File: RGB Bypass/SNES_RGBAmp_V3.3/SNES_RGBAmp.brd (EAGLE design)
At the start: 31 x 18.6 mm, 25 parts

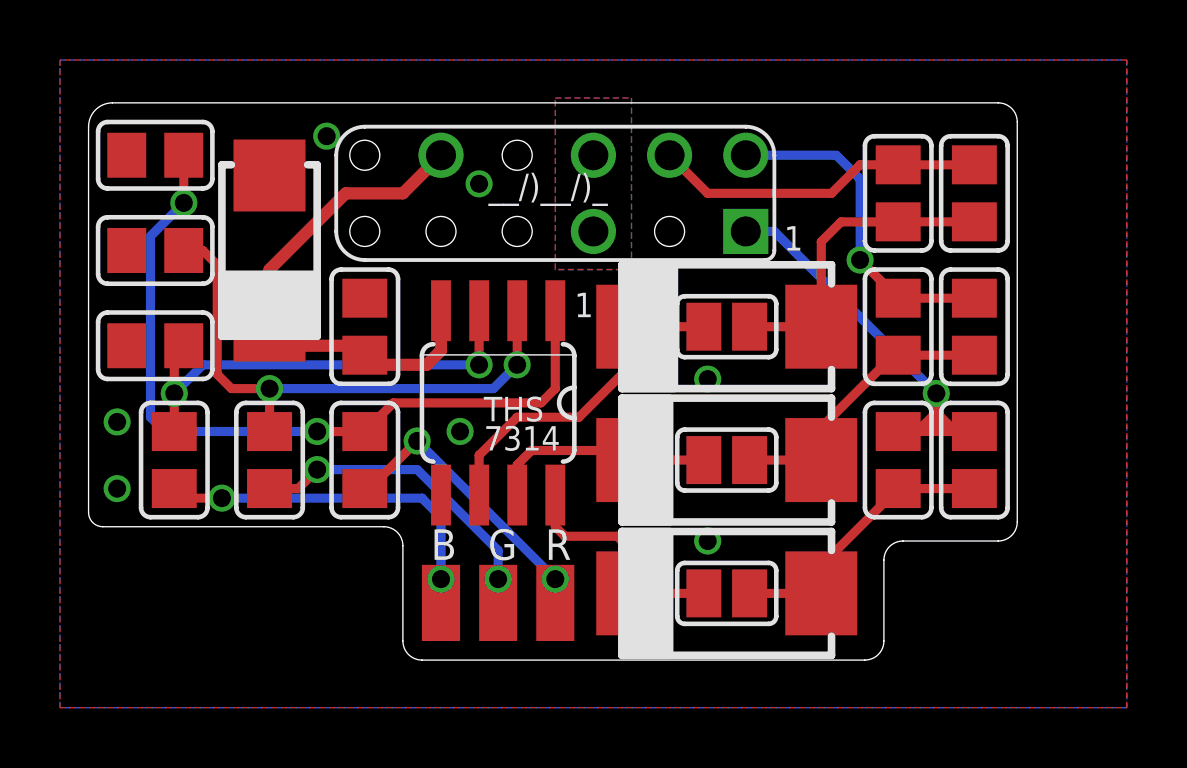
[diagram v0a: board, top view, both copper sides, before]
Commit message: RGB Bypass Version Update: - adjustment of wires - mirrored positioning of R, G and B pad - exact values for resistors - add a version with CSYNC-buffering (for 1Chip03 boards and later) - more detailed notes in README
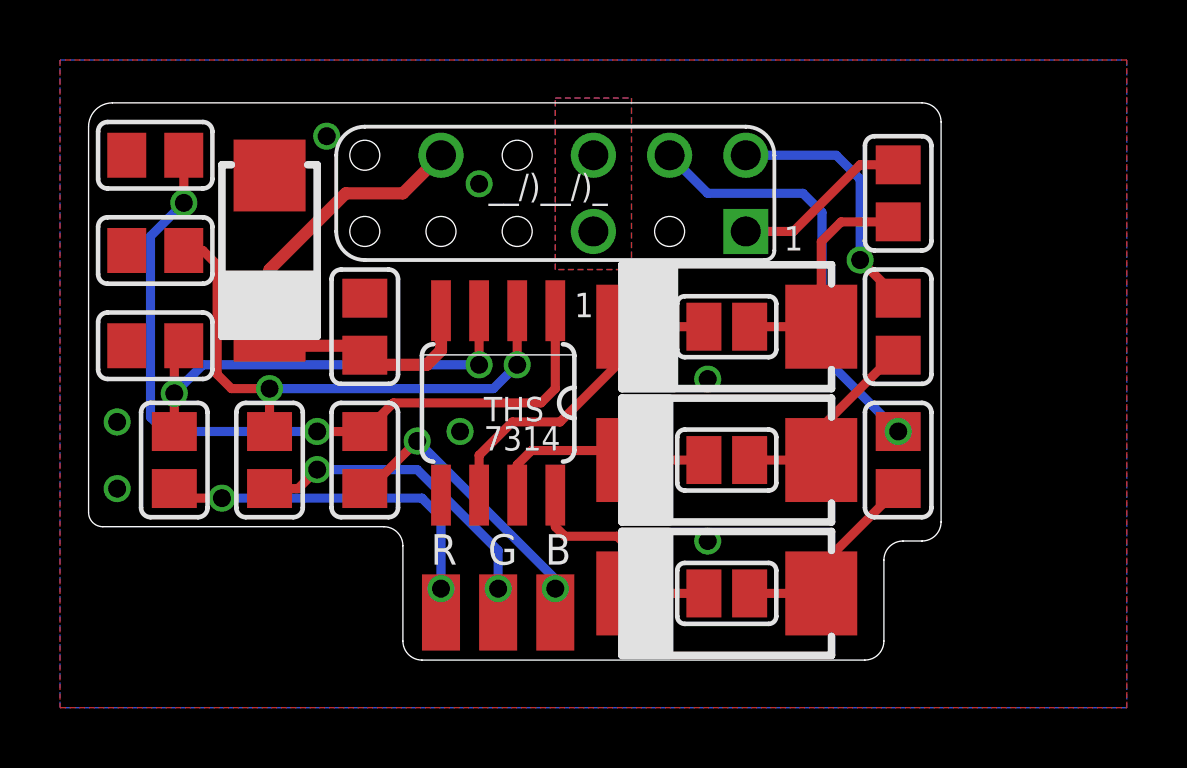
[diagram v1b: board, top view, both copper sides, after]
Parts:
- removed R7, R8, R9: 75, snescart:Z0805
- moved B 3.82 mm to (26.7, 24.8)
- moved R 3.82 mm to (22.9, 24.8)
- moved G 0.32 mm to (24.8, 24.8)
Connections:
- net N$13: no longer R8.1
- net N$14: now also B.1; no longer R.1
- net N$16: now also R.1; no longer B.1
- net N$4: no longer R9.1
- net N$5: now also U$2.P$4; no longer R9.2, U$2.P$1
- net N$6: no longer R8.2
- net N$8: no longer R7.1
- net N$9: now also U$2.P$1; no longer R7.2, U$2.P$4
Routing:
- net N$9: track 11.1 -> 6.00 mm
- net N$8: track 10.6 -> 8.06 mm
- net N$6: track 11.2 -> 8.64 mm
- net N$4: track 9.49 -> 6.95 mm
- net N$13: track 9.58 -> 7.04 mm
- net N$5: track 14.9 -> 14.2 mm
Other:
- board size 31 x 18.6 mm -> 28.4 x 18.6 mm
- board text added: "(1.3kΩ)"
- board text added: "(8.45kΩ)"
- board text added: "(806Ω)"
- board text added: "(9.53kΩ)"
- board text added: "R1-R3 (NTSC:75Ω ,PAL:39Ω)"
- board text added: "R4"
- board text added: "R5"
- board text added: "R6"
- board text added: "R7"
- board text added: "R8"
- board text added: "R9"
- board text added: "RGBAmp for SNES V3.3"
- board text removed: "(PAL cable)"
- board text removed: "(network for brightness- correction)"
- board text removed: "R1-R3 (75Ω)"
- board text removed: "R4-R6 (75Ω)"
- board text removed: "R7-R12"
- board text removed: "RGBAmp for SNES V3.1b"

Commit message: Update silkscreen
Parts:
- removed R10, R11, R12: 75, snescart:Z0805
- added R7: 9.53k, snescart:Z0805
- added R8, R9: 8.45k, snescart:Z0805
- R4: value 75 -> 806
- R5, R6: value 75 -> 1.3k
- moved R6 12.3 mm to (20.3, 29.8), turned to 270 degrees
- moved R5 7.96 mm to (17.1, 29.8), turned to 270 degrees
- moved R2 4.45 mm to (38.1, 34.3)
- moved R3 4.45 mm to (38.1, 29.8)
- moved R4 3.86 mm to (14.0, 29.8), turned to 270 degrees
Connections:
- net GND: now also R7.1, R8.1, R9.1; no longer R4.1, R5.1, R6.1
- net N$1: now also R6.1, R9.2; no longer R10.1, R6.2
- net N$13: now also R2.1; no longer R3.1
- net N$14: now also R6.2; no longer R10.2
- net N$15: now also R5.2; no longer R11.2
- net N$16: now also R4.2; no longer R12.2
- net N$2: now also R5.1, R8.2; no longer R11.1, R5.2
- net N$3: now also R4.1, R7.2; no longer R12.1, R4.2
- net N$4: now also R3.1; no longer R2.1
- net N$5: now also R3.2; no longer R2.2
- net N$6: now also R2.2; no longer R3.2
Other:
- board text added: "+"
